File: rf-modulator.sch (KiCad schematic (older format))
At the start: 16 parts, among them CN8 8 pin DIN, M1 RF_Modulator

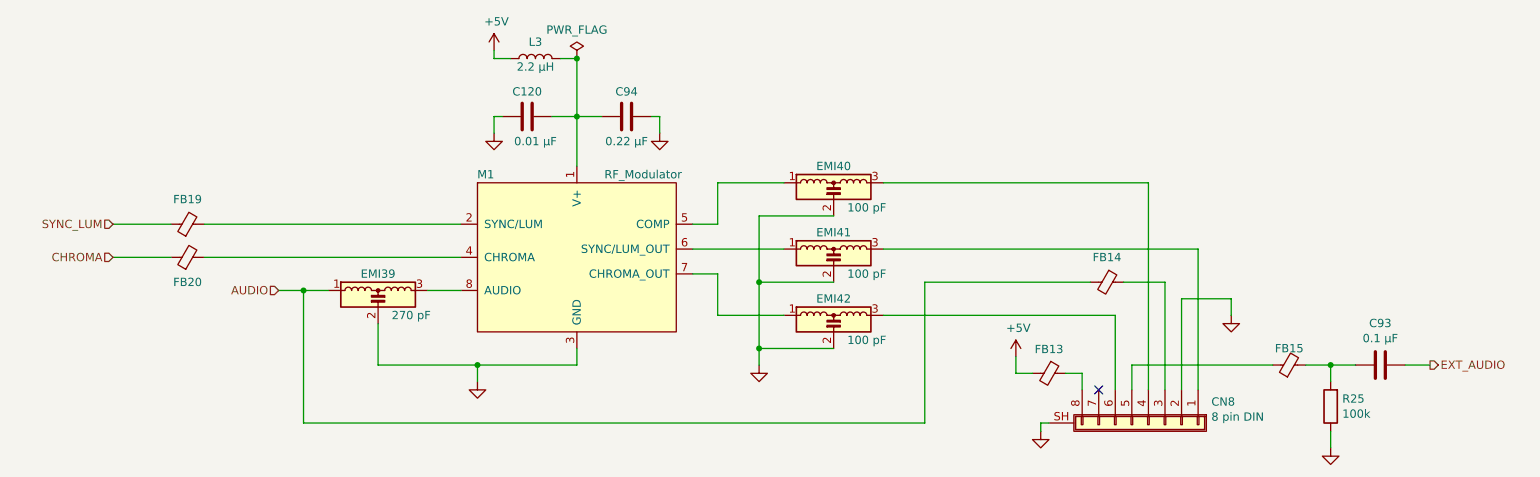
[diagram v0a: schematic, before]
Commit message: Clean up schematic
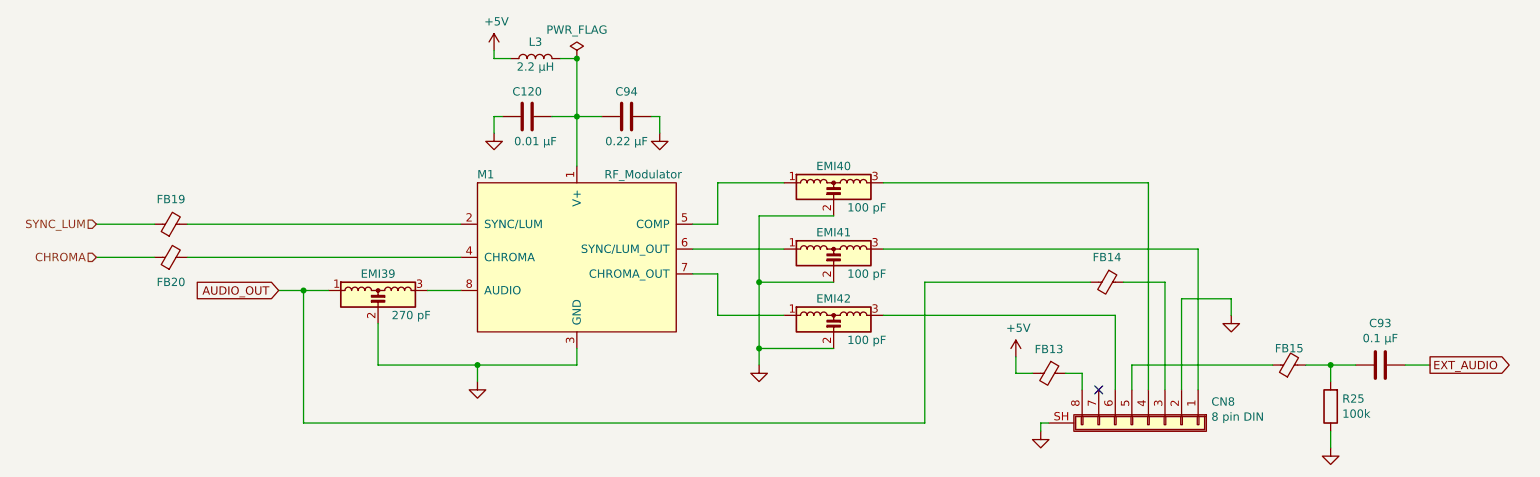
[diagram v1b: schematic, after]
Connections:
- net AUDIO renamed AUDIO_OUT
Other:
- moved on the sheet: FB19, FB20
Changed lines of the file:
@@
 	1    0    0    -1
 $EndComp
-Text HLabel 3600 3950 0    50   Input ~ 0
-AUDIO
-Text HLabel 2600 3550 0    50   Input ~ 0
+Text HLabel 2500 3550 0    50   Input ~ 0
 SYNC_LUM
-Text HLabel 2600 3750 0    50   Input ~ 0
+Text HLabel 2500 3750 0    50   Input ~ 0
 CHROMA
 Wire Wire Line
-	4700 3550 3150 3550
+	4700 3550 3050 3550
 $Comp
 L Device:EMI_Filter_LCL EMI39
@@
 $EndComp
 Wire Wire Line
-	2600 3750 2950 3750
+	2500 3750 2850 3750
 Wire Wire Line
 	3900 3950 3750 3950
@@
 	0    1    1    0
 $EndComp
-Text HLabel 10550 4400 2    50   Output ~ 0
-EXT_AUDIO
 Wire Wire Line
 	10550 4400 10400 4400
@@
 L Open128:Ferrite_Bead FB19
 U 1 1 5DCF0C3A
-P 3050 3550
-F 0 "FB19" V 3200 3550 50  0000 C CNN
-F 1 "Ferrite_Bead_Small" V 2904 3550 50  0001 C CNN
-F 2 "Open128:Ferrite_Bead_vertical" V 2980 3550 50  0001 C CNN
-F 3 "~" H 3050 3550 50  0001 C CNN
-F 4 "81-BL02RN2R1M2B" H 3050 3550 50  0001 C CNN "Mouser Part"
-	1    3050 3550
+P 2950 3550
+F 0 "FB19" V 3100 3550 50  0000 C CNN
+F 1 "Ferrite_Bead_Small" V 2804 3550 50  0001 C CNN
+F 2 "Open128:Ferrite_Bead_vertical" V 2880 3550 50  0001 C CNN
+F 3 "~" H 2950 3550 50  0001 C CNN
+F 4 "81-BL02RN2R1M2B" H 2950 3550 50  0001 C CNN "Mouser Part"
+	1    2950 3550
 	0    -1   -1   0
 $EndComp
 Wire Wire Line
-	2950 3550 2600 3550
+	2850 3550 2500 3550
 $Comp
 L Open128:Ferrite_Bead FB20
 U 1 1 5DCF15D6
-P 3050 3750
-F 0 "FB20" V 2900 3750 50  0000 C CNN
-F 1 "Ferrite_Bead_Small" V 2904 3750 50  0001 C CNN
-F 2 "Open128:Ferrite_Bead_vertical" V 2980 3750 50  0001 C CNN
-F 3 "~" H 3050 3750 50  0001 C CNN
-F 4 "81-BL02RN2R1M2B" H 3050 3750 50  0001 C CNN "Mouser Part"
-	1    3050 3750
+P 2950 3750
+F 0 "FB20" V 2800 3750 50  0000 C CNN
+F 1 "Ferrite_Bead_Small" V 2804 3750 50  0001 C CNN
+F 2 "Open128:Ferrite_Bead_vertical" V 2880 3750 50  0001 C CNN
+F 3 "~" H 2950 3750 50  0001 C CNN
+F 4 "81-BL02RN2R1M2B" H 2950 3750 50  0001 C CNN "Mouser Part"
+	1    2950 3750
 	0    -1   -1   0
 $EndComp
 Wire Wire Line
-	3150 3750 4700 3750
+	3050 3750 4700 3750
 $Comp
 L Device:L L?
@@
 Wire Wire Line
 	8200 4750 8200 4800
+Text GLabel 10550 4400 2    50   Output ~ 0
+EXT_AUDIO
+Text GLabel 3600 3950 0    50   Input ~ 0
+AUDIO_OUT
 $EndSCHEMATC
